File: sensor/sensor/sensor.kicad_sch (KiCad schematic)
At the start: 13 parts, among them J1 RJ12_Shielded, J2 Conn_01x04, J3 Conn_01x06, U1 PCA9615DP, U2 LTC4316xDD, U3 APDS-9960, U4 TPS76301

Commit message: update sensor
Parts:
- added C1: 1n, symbol Device:C
- added C2, C3: 1u, symbol Device:C
- added R10: 52k, symbol Device:R
- added R11: 30k, symbol Device:R
- added R12, R13, R7, R8: 4.7k, symbol Device:R
- added R9: 10k, symbol Device:R
- added U5: TPS73101DBV, Package_TO_SOT_SMD:SOT-23-5, symbol Regulator_Linear:TPS73101DBV
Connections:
- net +3.3V: now also U2.4 (V_{CC}), U2.5 (ENABLE), C1.1, C2.1, R10.1, R12.1, R13.1, R7.1, R8.1, R9.1, U5.5 (OUT)
- net +5V: now also J1.1, J2.2 (Pin_2), J3.1 (Pin_1), C3.1, U5.1 (IN), U5.3 (EN)
- net GND: now also J1.6, J2.1 (Pin_1), J3.6 (Pin_6), U1.5 (V_{SS}), U2.1 (GND), C2.2, C3.2, R11.2, U5.2 (GND)
- net at U2.10 (SCLIN): now also J2.4 (Pin_4), U1.4 (SCL), R12.2, R8.2
- net at U2.7 (SDAIN): now also J2.3 (Pin_3), U1.2 (SDA), R13.2, R7.2
- net at R1.2, R2.2, U1.8 (DSDAP): now also J1.2, J3.2 (Pin_2)
- net at J3.3 (Pin_3): now also J1.3, R2.1, R3.1, U1.9 (DSDAM)
- net at J3.4 (Pin_4): now also J1.4, R4.2, R5.2, U1.7 (DSCLP)
- net at J3.5 (Pin_5): now also J1.5, R5.1, R6.1, U1.6 (DSCLM)
- net at U1.3 (EN): now also R9.2
- new net: C1.2, R10.2, R11.1, U5.4 (FB)
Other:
- note added: "For 2.5v R1=40k R2=37k"
- note added: "For 3.3v R1=52k R2=30k"
- moved on the sheet: J1, J2, J3, R1, R2, R3, R4, R5, R6, U1, U2, U3

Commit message: updated sensor
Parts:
- removed R12, R13: 4.7k, symbol Device:R
- removed U3: APDS-9960, Sensor:Avago_APDS-9960, symbol Sensor:APDS-9960
- added R14: 10k, symbol Device:R
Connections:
- net +3.3V: now also R14.1; no longer U2.5 (ENABLE)
- net GND: now also U2.11 (EP)
- net sda: now reaches U2.8 (SDAOUT)
- net scl: now reaches U2.9 (SCLOUT)
- new net: R14.2, U2.5 (ENABLE)
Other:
- added sheet Sensors (sensors.kicad_sch)
- moved on the sheet: U2

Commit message: karmanyaah's footprints
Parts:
- C1, C2, C3: footprint (none) -> Capacitor_SMD:C_0603_1608Metric_Pad1.08x0.95mm_HandSolder
- J1: footprint Connector_RJ:RJ25_Wayconn_MJEA-660X1_Horizontal -> (none)
- J2, J3: footprint (none) -> Connector_JST:JST_SH_SM03B-SRSS-TB_1x03-1MP_P1.00mm_Horizontal
- R1, R10, R11, R14, R2, R3, R4, R5, R6, R7, R8, R9: footprint (none) -> Resistor_SMD:R_0603_1608Metric_Pad0.98x0.95mm_HandSolder
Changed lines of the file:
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@@
 			)
 		)
-		(property "Footprint" ""
+		(property "Footprint" "Resistor_SMD:R_0603_1608Metric_Pad0.98x0.95mm_HandSolder"
 			(at 172.212 87.63 90)
 			(effects
@@
 			)
 		)
-		(property "Footprint" ""
+		(property "Footprint" "Capacitor_SMD:C_0603_1608Metric_Pad1.08x0.95mm_HandSolder"
 			(at 30.1752 177.8 0)
 			(effects
@@
 			)
 		)
-		(property "Footprint" ""
+		(property "Footprint" "Connector_JST:JST_SH_SM03B-SRSS-TB_1x03-1MP_P1.00mm_Horizontal"
 			(at 254 107.95 0)
 			(effects
@@
 			)
 		)
-		(property "Footprint" ""
+		(property "Footprint" "Resistor_SMD:R_0603_1608Metric_Pad0.98x0.95mm_HandSolder"
 			(at 188.468 114.3 90)
 			(effects
@@
 			)
 		)
-		(property "Footprint" ""
+		(property "Footprint" "Capacitor_SMD:C_0603_1608Metric_Pad1.08x0.95mm_HandSolder"
 			(at 84.7852 177.8 0)
 			(effects
@@
 			)
 		)
-		(property "Footprint" ""
+		(property "Footprint" "Resistor_SMD:R_0603_1608Metric_Pad0.98x0.95mm_HandSolder"
 			(at 184.912 106.68 90)
 			(effects
@@
 			)
 		)
-		(property "Footprint" ""
+		(property "Footprint" "Resistor_SMD:R_0603_1608Metric_Pad0.98x0.95mm_HandSolder"
 			(at 122.682 109.22 90)
 			(effects
@@
 			)
 		)
-		(property "Footprint" ""
+		(property "Footprint" "Resistor_SMD:R_0603_1608Metric_Pad0.98x0.95mm_HandSolder"
 			(at 172.212 102.87 90)
 			(effects
@@
 			)
 		)
-		(property "Footprint" ""
+		(property "Footprint" "Resistor_SMD:R_0603_1608Metric_Pad0.98x0.95mm_HandSolder"
 			(at 175.768 95.25 90)
 			(effects
@@
 			)
 		)
-		(property "Footprint" ""
+		(property "Footprint" "Capacitor_SMD:C_0603_1608Metric_Pad1.08x0.95mm_HandSolder"
 			(at 75.8952 177.8 0)
 			(effects
@@
 			)
 		)
-		(property "Footprint" "Connector_RJ:RJ25_Wayconn_MJEA-660X1_Horizontal"
+		(property "Footprint" ""
 			(at 223.52 108.585 90)
 			(effects
@@
 			)
 		)
-		(property "Footprint" ""
+		(property "Footprint" "Resistor_SMD:R_0603_1608Metric_Pad0.98x0.95mm_HandSolder"
 			(at 62.992 184.15 90)
 			(effects
@@
 			)
 		)
-		(property "Footprint" ""
+		(property "Footprint" "Resistor_SMD:R_0603_1608Metric_Pad0.98x0.95mm_HandSolder"
 			(at 117.602 104.14 90)
 			(effects
@@
 			)
 		)
-		(property "Footprint" ""
+		(property "Footprint" "Connector_JST:JST_SH_SM03B-SRSS-TB_1x03-1MP_P1.00mm_Horizontal"
 			(at 118.11 127 0)
 			(effects
@@
 			)
 		)
-		(property "Footprint" ""
+		(property "Footprint" "Resistor_SMD:R_0603_1608Metric_Pad0.98x0.95mm_HandSolder"
 			(at 99.822 93.98 90)
 			(effects
@@
 			)
 		)
-		(property "Footprint" ""
+		(property "Footprint" "Resistor_SMD:R_0603_1608Metric_Pad0.98x0.95mm_HandSolder"
 			(at 62.992 173.99 90)
 			(effects
@@
 			)
 		)
-		(property "Footprint" ""
+		(property "Footprint" "Resistor_SMD:R_0603_1608Metric_Pad0.98x0.95mm_HandSolder"
 			(at 184.912 121.92 90)
 			(effects
@@
 			)
 		)
-		(property "Footprint" ""
+		(property "Footprint" "Resistor_SMD:R_0603_1608Metric_Pad0.98x0.95mm_HandSolder"
 			(at 133.35 104.648 90)
 			(effects

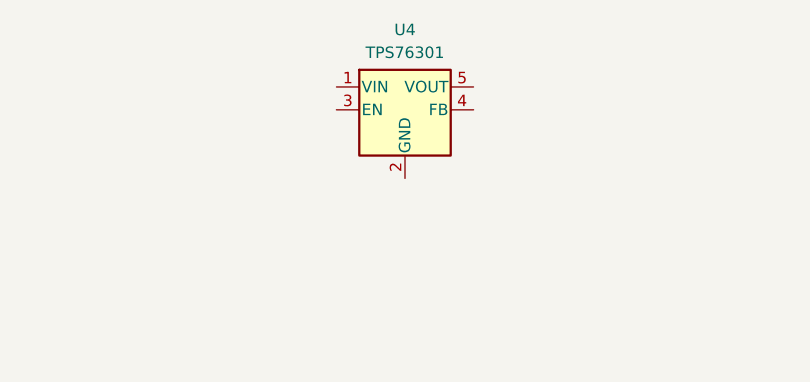
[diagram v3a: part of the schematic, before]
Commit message: added RJ12 footprint to sensor
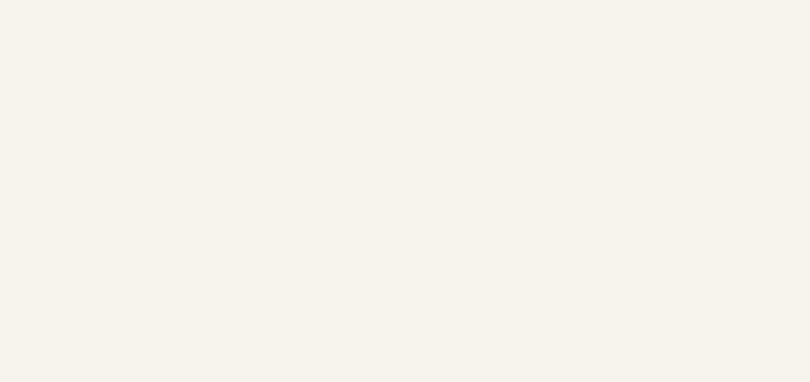
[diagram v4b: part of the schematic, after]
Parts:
- removed U4: TPS76301, Package_TO_SOT_SMD:SOT-23-5, symbol Regulator_Linear:TPS76301
- J1: footprint (none) -> RJ12_Pin_Connector:RJ12_Pin_Connector
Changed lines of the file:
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@@
 			)
 		)
-		(property "Footprint" ""
+		(property "Footprint" "RJ12_Pin_Connector:RJ12_Pin_Connector"
 			(at 223.52 108.585 90)
 			(effects
@@
 					(unit 1)
 				)
-			)
-		)
-	)
-	(symbol
-		(lib_id "Regulator_Linear:TPS76301")
-		(at 160.02 43.18 0)
-		(unit 1)
-		(exclude_from_sim no)
-		(in_bom yes)
-		(on_board yes)
-		(dnp no)
-		(fields_autoplaced yes)
-		(property "Reference" "U4"
-			(at 160.02 34.29 0)
-			(effects
-				(font
-					(size 1.27 1.27)
-				)
-			)
-		)
-		(property "Value" "TPS76301"
-			(at 160.02 36.83 0)
-			(effects
-				(font
-					(size 1.27 1.27)
-				)
-			)
-		)
-		(property "Footprint" "Package_TO_SOT_SMD:SOT-23-5"
-			(at 160.02 34.925 0)
-			(effects
-				(font
-					(size 1.27 1.27)
-					(italic yes)
-				)
-				(hide yes)
-			)
-		)
-		(property "Datasheet" "http://www.ti.com/lit/ds/symlink/tps763.pdf"
-			(at 160.02 43.18 0)
-			(effects
-				(font
-					(size 1.27 1.27)
-				)
-				(hide yes)
-			)
-		)
-		(property "Description" "Low power 150mA LDO variable output voltage, SOT-23-5"
-			(at 160.02 43.18 0)
-			(effects
-				(font
-					(size 1.27 1.27)
-				)
-				(hide yes)
-			)
-		)
-		(pin "2"
-		)
-		(pin "5"
-		)
-		(pin "1"
-		)
-		(pin "3"
-		)
-		(pin "4"
-		)
-		(instances
-			(project ""
-				(path "/46f6a130-b02e-4523-867c-7812ad0e1543"
-					(reference "U4")
-					(unit 1)
-				)

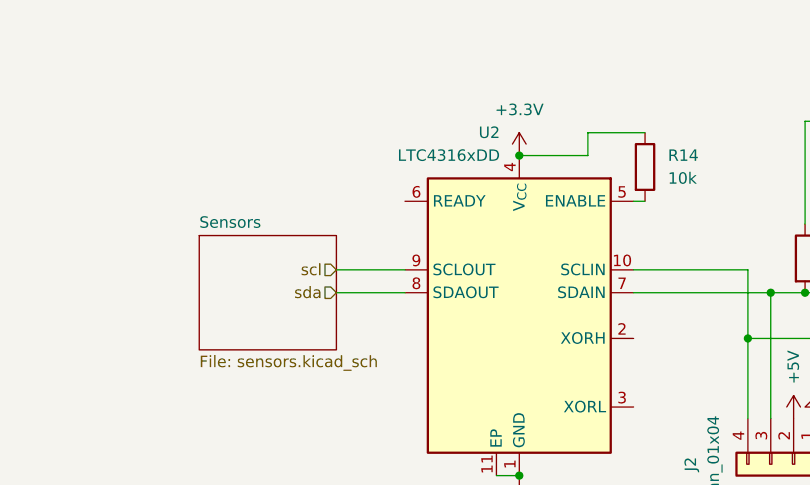
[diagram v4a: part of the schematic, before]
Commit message: new tca9536 footprint
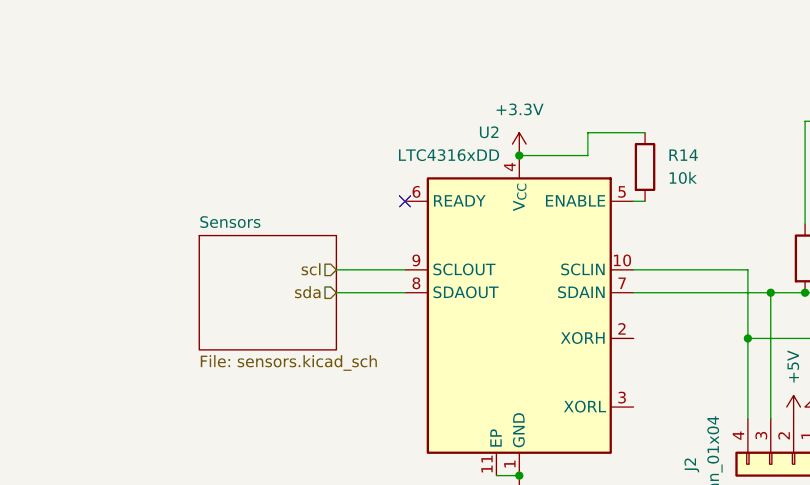
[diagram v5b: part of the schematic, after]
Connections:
- no-connect marks 0 -> 1
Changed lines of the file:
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@@
 		(color 0 0 0 0)
+	)
+	(no_connect
+		(at 74.93 97.79)
 	)
 	(wire

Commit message: remerge
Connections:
- net GND: now also U2.2 (XORH)
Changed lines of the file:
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@@
+	(wire
+		(pts
+			(xy 100.33 113.03) (xy 105.41 113.03)
+		)
+		(stroke
+			(width 0)
+			(type default)
+		)
+	)
 	(wire
 		(pts
@@
 					(unit 1)
 				)
+			)
+		)
+	)
+	(symbol
+		(lib_id "power:GND")
+		(at 105.41 113.03 0)
+		(unit 1)
+		(exclude_from_sim no)
+		(in_bom yes)
+		(on_board yes)
+		(dnp no)
+		(fields_autoplaced yes)
+		(property "Reference" "#PWR042"
+			(at 105.41 119.38 0)
+			(effects
+				(font
+					(size 1.27 1.27)
+				)
+				(hide yes)
+			)
+		)
+		(property "Value" "GND"
+			(at 105.41 118.11 0)
+			(effects
+				(font
+					(size 1.27 1.27)
+				)
+			)
+		)
+		(property "Footprint" ""
+			(at 105.41 113.03 0)
+			(effects
+				(font
+					(size 1.27 1.27)
+				)
+				(hide yes)
+			)
+		)
+		(property "Datasheet" ""
+			(at 105.41 113.03 0)
+			(effects
+				(font
+					(size 1.27 1.27)
+				)
+				(hide yes)
+			)
+		)
+		(property "Description" "Power symbol creates a global label with name \"GND\" , ground"
+			(at 105.41 113.03 0)
+			(effects
+				(font
+					(size 1.27 1.27)
+				)
+				(hide yes)
+			)
+		)
+		(pin "1"
+		)
+		(instances
+			(project ""
+				(path "/46f6a130-b02e-4523-867c-7812ad0e1543"
+					(reference "#PWR042")
+					(unit 1)
+				)
